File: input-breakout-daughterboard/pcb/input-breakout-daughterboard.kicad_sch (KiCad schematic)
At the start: 3 parts

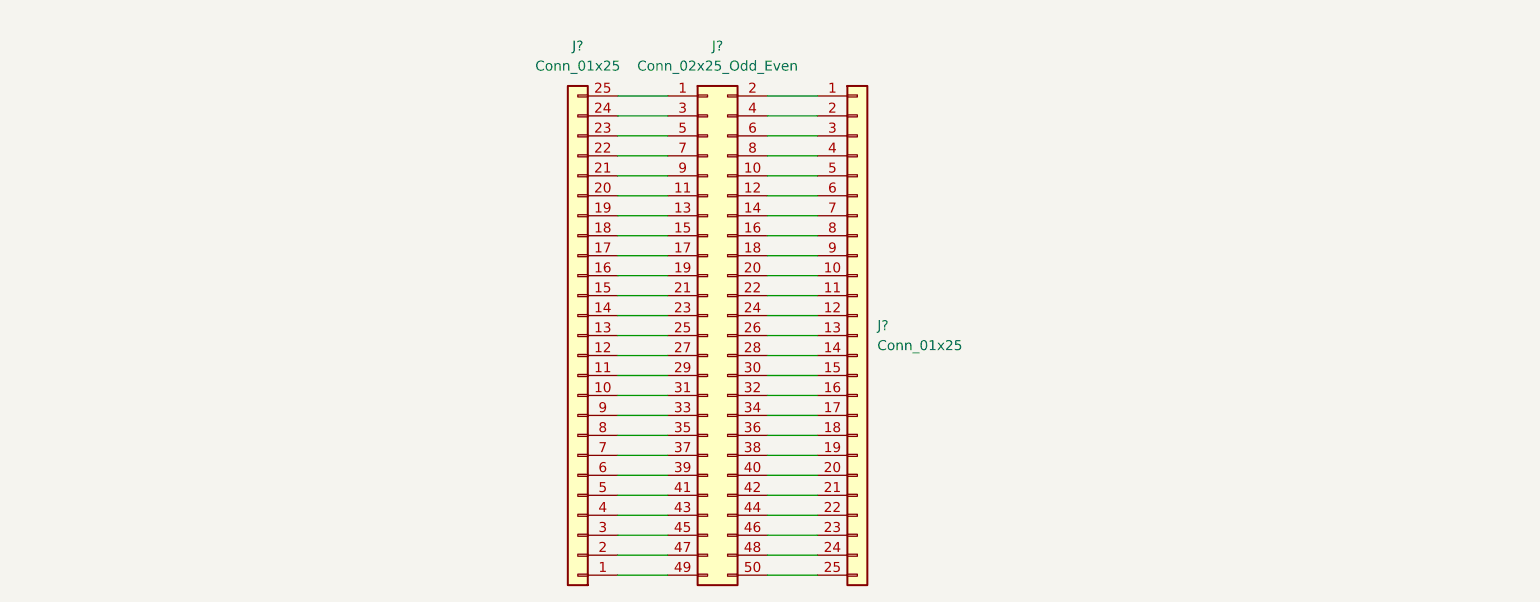
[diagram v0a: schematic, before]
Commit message: input seems good enough for a v1
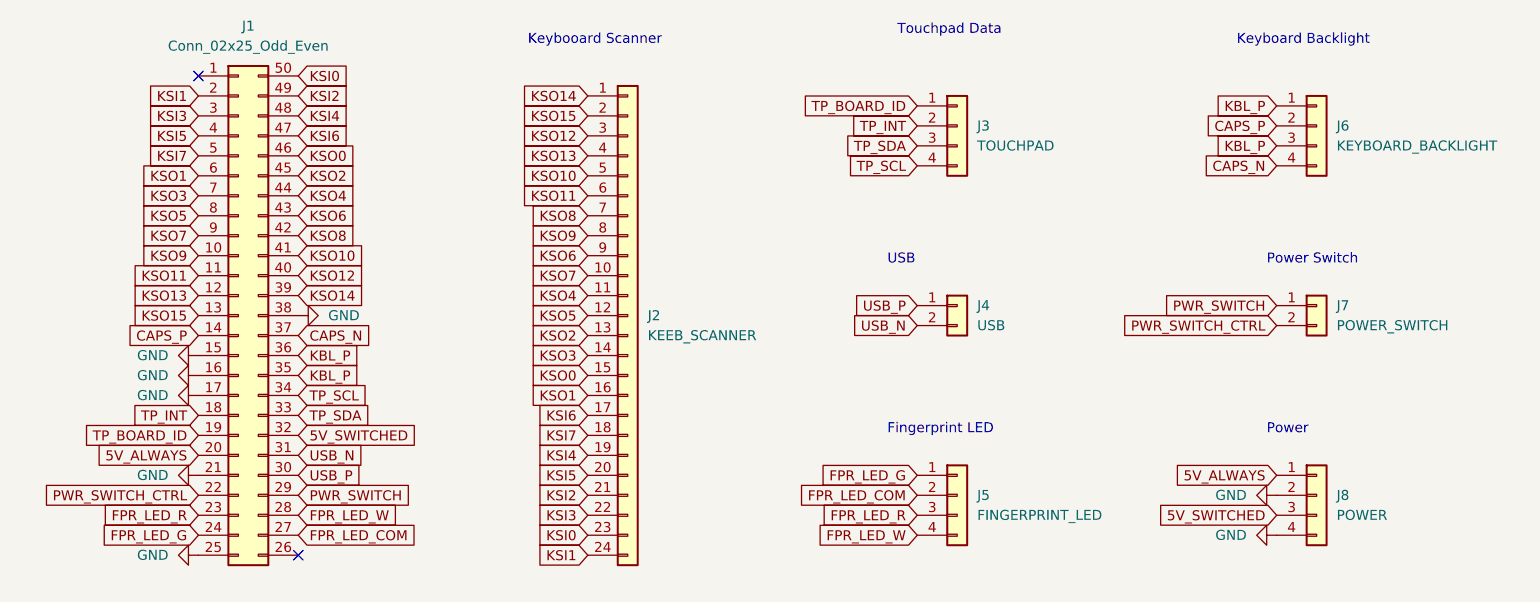
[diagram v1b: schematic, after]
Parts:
- removed J? (x2): Conn_01x25, symbol Connector_Generic:Conn_01x25
- added J2: KEEB_SCANNER, Connector_PinSocket_2.54mm:PinSocket_2x12_P2.54mm_Vertical, symbol Connector_Generic:Conn_01x24
- added J3: TOUCHPAD, Connector_PinSocket_2.54mm:PinSocket_2x02_P2.54mm_Vertical, symbol Connector_Generic:Conn_01x04
- added J4: USB, Connector_PinSocket_2.54mm:PinSocket_1x02_P2.54mm_Vertical, symbol Connector_Generic:Conn_01x02
- added J5: FINGERPRINT_LED, Connector_PinSocket_2.54mm:PinSocket_2x02_P2.54mm_Vertical, symbol Connector_Generic:Conn_01x04
- added J6: KEYBOARD_BACKLIGHT, Connector_PinSocket_2.54mm:PinSocket_2x02_P2.54mm_Vertical, symbol Connector_Generic:Conn_01x04
- added J7: POWER_SWITCH, Connector_PinSocket_2.54mm:PinSocket_1x02_P2.54mm_Vertical, symbol Connector_Generic:Conn_01x02
- added J8: POWER, Connector_PinSocket_2.54mm:PinSocket_2x02_P2.54mm_Vertical, symbol Connector_Generic:Conn_01x04
- J1: renamed from J?; footprint (none) -> footprints:10156001-051100LF; symbol Connector_Generic:Conn_02x25_Odd_Even -> Connector_Generic:Conn_02x25_Counter_Clockwise
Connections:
- net KSO9: now reaches J1.10 (Pin_10)
- net KSO9: now also J2.8 (Pin_8)
- net KSO11: now reaches J1.11 (Pin_11)
- net KSO11: now also J2.6 (Pin_6)
- net KSO13: now reaches J1.12 (Pin_12)
- net KSO13: now also J2.4 (Pin_4)
- net KSO15: now reaches J1.13 (Pin_13)
- net KSO15: now also J2.2 (Pin_2)
- net CAPS_P: now reaches J1.14 (Pin_14)
- net CAPS_P: now also J6.2 (Pin_2)
- net GND: now reaches J1.15 (Pin_15)
- net GND: now also J1.16 (Pin_16), J1.17 (Pin_17), J1.21 (Pin_21), J1.25 (Pin_25), J1.38 (Pin_38), J8.2 (Pin_2), J8.4 (Pin_4)
- net TP_INT: now reaches J1.18 (Pin_18)
- net TP_INT: now also J3.2 (Pin_2)
- net TP_BOARD_ID: now reaches J1.19 (Pin_19)
- net TP_BOARD_ID: now also J3.1 (Pin_1)
- net KSI1: now reaches J1.2 (Pin_2)
- net KSI1: now also J2.24 (Pin_24)
- net 5V_ALWAYS: now reaches J1.20 (Pin_20)
- net 5V_ALWAYS: now also J8.1 (Pin_1)
- net PWR_SWITCH_CTRL: now reaches J1.22 (Pin_22)
- net PWR_SWITCH_CTRL: now also J7.2 (Pin_2)
- net FPR_LED_R: now reaches J1.23 (Pin_23)
- net FPR_LED_R: now also J5.3 (Pin_3)
- net FPR_LED_G: now reaches J1.24 (Pin_24)
- net FPR_LED_G: now also J5.1 (Pin_1)
- net FPR_LED_COM: now reaches J1.27 (Pin_27)
- net FPR_LED_COM: now also J5.2 (Pin_2)
- net FPR_LED_W: now reaches J1.28 (Pin_28)
- net FPR_LED_W: now also J5.4 (Pin_4)
- net PWR_SWITCH: now reaches J1.29 (Pin_29)
- net PWR_SWITCH: now also J7.1 (Pin_1)
- net KSI3: now reaches J1.3 (Pin_3)
- net KSI3: now also J2.22 (Pin_22)
- net USB_P: now reaches J1.30 (Pin_30)
- net USB_P: now also J4.1 (Pin_1)
- net USB_N: now reaches J1.31 (Pin_31)
- net USB_N: now also J4.2 (Pin_2)
- net 5V_SWITCHED: now reaches J1.32 (Pin_32)
- net 5V_SWITCHED: now also J8.3 (Pin_3)
- net TP_SDA: now reaches J1.33 (Pin_33)
- net TP_SDA: now also J3.3 (Pin_3)
- net TP_SCL: now reaches J1.34 (Pin_34)
- net TP_SCL: now also J3.4 (Pin_4)
- net KBL_P: now reaches J1.35 (Pin_35)
- net KBL_P: now also J1.36 (Pin_36), J6.1 (Pin_1), J6.3 (Pin_3)
- net CAPS_N: now reaches J1.37 (Pin_37)
- net CAPS_N: now also J6.4 (Pin_4)
- net KSO14: now reaches J1.39 (Pin_39)
- net KSO14: now also J2.1 (Pin_1)
- net KSI5: now reaches J1.4 (Pin_4)
- net KSI5: now also J2.20 (Pin_20)
- net KSO12: now reaches J1.40 (Pin_40)
- net KSO12: now also J2.3 (Pin_3)
- net KSO10: now reaches J1.41 (Pin_41)
- net KSO10: now also J2.5 (Pin_5)
- net KSO8: now reaches J1.42 (Pin_42)
- net KSO8: now also J2.7 (Pin_7)
- net KSO6: now reaches J1.43 (Pin_43)
- net KSO6: now also J2.9 (Pin_9)
- net KSO4: now reaches J1.44 (Pin_44)
- net KSO4: now also J2.11 (Pin_11)
- net KSO2: now reaches J1.45 (Pin_45)
- net KSO2: now also J2.13 (Pin_13)
- net KSO0: now reaches J1.46 (Pin_46)
- net KSO0: now also J2.15 (Pin_15)
- net KSI6: now reaches J1.47 (Pin_47)
- net KSI6: now also J2.17 (Pin_17)
- net KSI4: now reaches J1.48 (Pin_48)
- net KSI4: now also J2.19 (Pin_19)
- net KSI2: now reaches J1.49 (Pin_49)
- net KSI2: now also J2.21 (Pin_21)
- net KSI7: now reaches J1.5 (Pin_5)
- net KSI7: now also J2.18 (Pin_18)
- net KSI0: now reaches J1.50 (Pin_50)
- net KSI0: now also J2.23 (Pin_23)
- net KSO1: now reaches J1.6 (Pin_6)
- net KSO1: now also J2.16 (Pin_16)
- net KSO3: now reaches J1.7 (Pin_7)
- net KSO3: now also J2.14 (Pin_14)
- net KSO5: now reaches J1.8 (Pin_8)
- net KSO5: now also J2.12 (Pin_12)
- net KSO7: now reaches J1.9 (Pin_9)
- net KSO7: now also J2.10 (Pin_10)
- no-connect marks 0 -> 2
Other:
- note added: "Fingerprint LED"
- note added: "Keyboard Backlight"
- note added: "Keybooard Scanner"
- note added: "Power"
- note added: "Power Switch"
- note added: "Touchpad Data"
- note added: "USB"
- moved on the sheet: J1
